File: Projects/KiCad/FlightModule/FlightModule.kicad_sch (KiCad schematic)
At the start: 45 parts, among them J1 Conn_01x04_Pin, J2 Conn_01x04_Socket, J3 Conn_01x02_Pin, J4 Conn_01x02_Pin, J5 Conn_01x02_Pin, J6 Conn_01x02_Pin, Q2 DTC143E, SW1 SW_Push, U1 NUCLEO-F303K8, U2 MCP2562-E-P, U3 TLP222A, U4 TLP222A, U5 24LC1025, U6 24LC1025

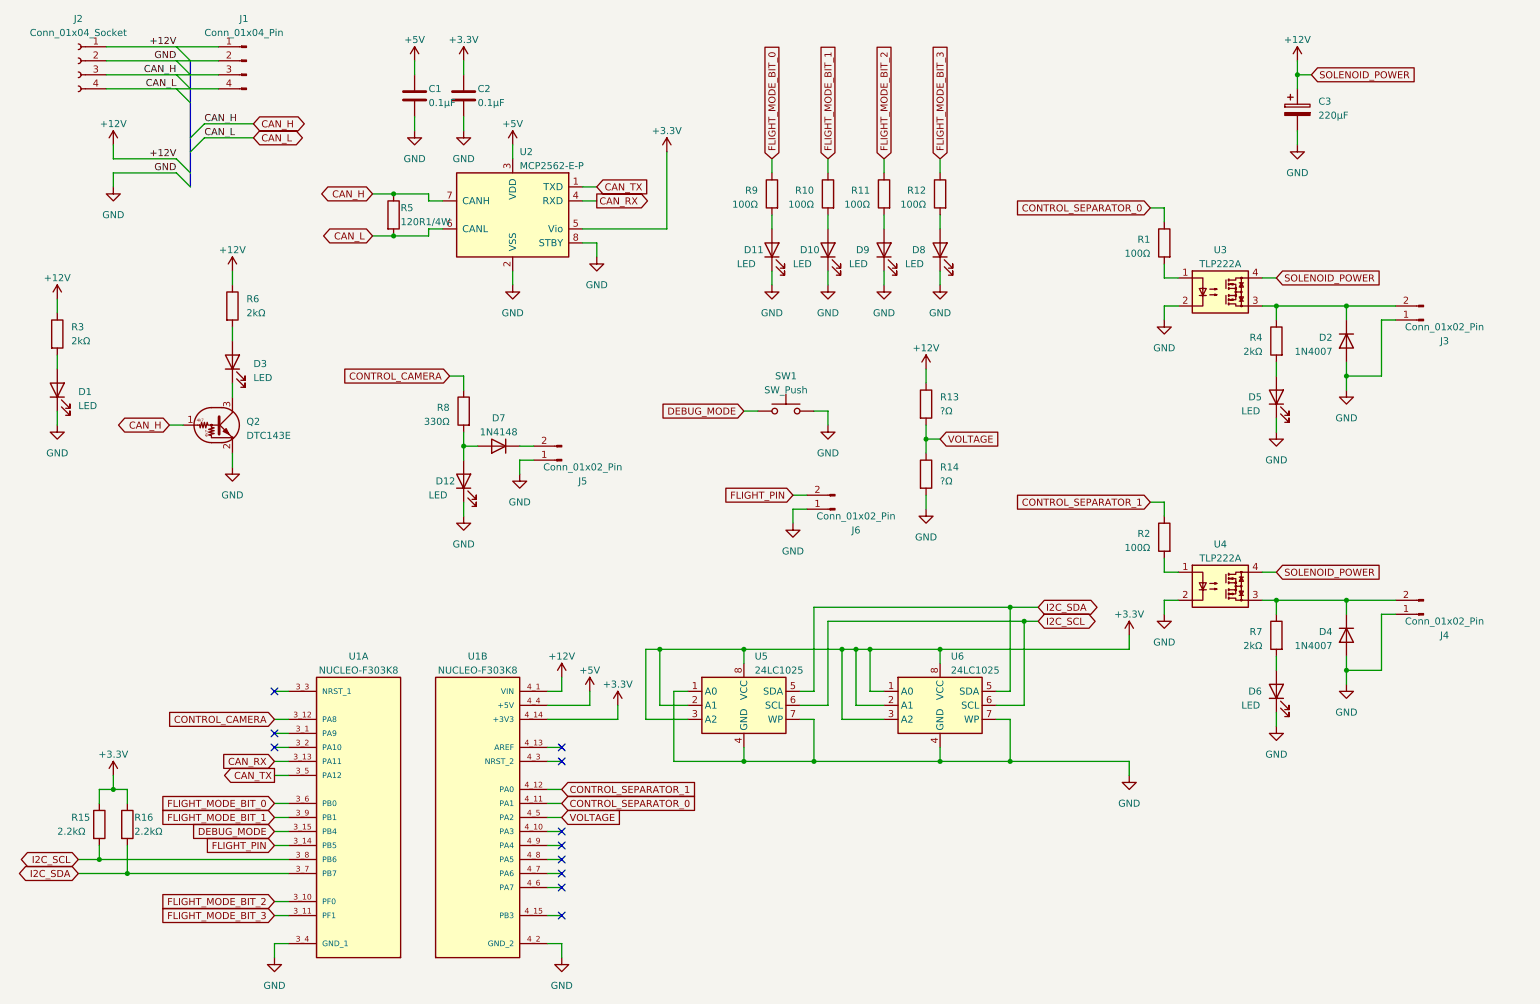
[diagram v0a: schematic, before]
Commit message: バスパワーのピンヘッダをP1.27からP2.54に修正
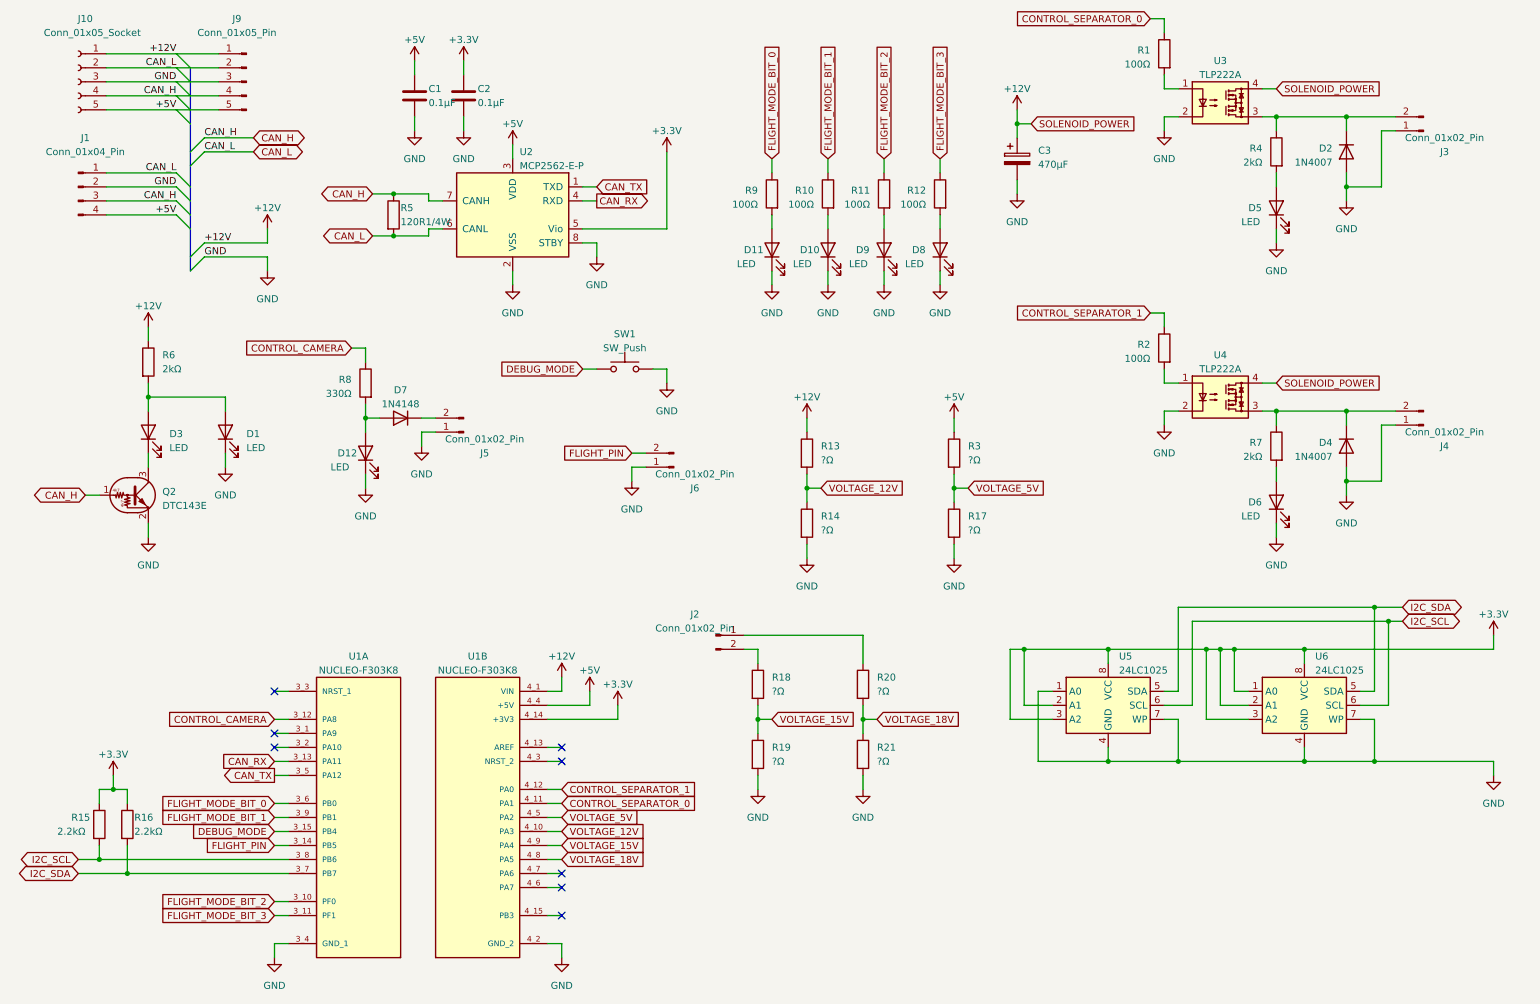
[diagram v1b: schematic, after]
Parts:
- removed J2: Conn_01x04_Socket, Connector_PinSocket_1.27mm:PinSocket_1x04_P1.27mm_Vertical, symbol Connector:Conn_01x04_Socket
- added J10: Conn_01x05_Socket, Connector_PinSocket_2.54mm:PinSocket_1x05_P2.54mm_Vertical, symbol Connector:Conn_01x05_Socket
- added J2: Conn_01x02_Pin, Connector_JST:JST_EH_S2B-EH_1x02_P2.50mm_Horizontal, symbol Connector:Conn_01x02_Pin
- added J9: Conn_01x05_Pin, Connector_PinHeader_2.54mm:PinHeader_1x05_P2.54mm_Vertical, symbol Connector:Conn_01x05_Pin
- added R17, R18, R19, R20, R21: ?Ω, Resistor_SMD:R_0805_2012Metric_Pad1.20x1.40mm_HandSolder, symbol Device:R
- C3: value 220μF -> 470μF; footprint Capacitor_SMD:CP_Elec_6.3x7.7 -> Capacitor_THT:CP_Radial_D10.0mm_P3.50mm
- J1: footprint Connector_PinHeader_1.27mm:PinHeader_1x04_P1.27mm_Vertical -> Connector_JST:JST_XH_S4B-XH-A_1x04_P2.50mm_Horizontal
- R3: value 2kΩ -> ?Ω
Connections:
- net +12V: now also J10.1 (Pin_1), J9.1 (Pin_1); no longer J1.1 (Pin_1), R3.1
- net +5V: now also J1.4 (Pin_4), R3.1, J10.5 (Pin_5), J9.5 (Pin_5)
- net CAN_H: now also J10.4 (Pin_4), J9.4 (Pin_4)
- net CAN_L: now also J1.1 (Pin_1), J10.2 (Pin_2), J9.2 (Pin_2); no longer J1.4 (Pin_4)
- net GND: now also J10.3 (Pin_3), J9.3 (Pin_3), R17.2, R19.2, R21.2
- net at D3.2 (A), R6.2: now also D1.2 (A)
- net VOLTAGE_5V: now reaches R3.2
- net VOLTAGE_5V: now also U1.4_5 (PA2), R17.1; no longer D1.2 (A)
- net VOLTAGE_12V: now reaches U1.4_10 (PA3)
- net VOLTAGE_12V: now also R13.2, R14.1
- net VOLTAGE_18V: now reaches U1.4_8 (PA5)
- net VOLTAGE_18V: now also R20.2, R21.1
- net VOLTAGE_15V: now reaches U1.4_9 (PA4)
- net VOLTAGE_15V: now also R18.2, R19.1
- removed net VOLTAGE: R13.2, R14.1, U1.4_5 (PA2)
- new net: J2.2 (Pin_2), R18.1
- new net: J2.1 (Pin_1), R20.1
- no-connect marks 11 -> 8
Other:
- moved on the sheet: C3, D1, D12, D2, D3, D4, D5, D6, D7, J3, J4, J5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

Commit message: RCを解決
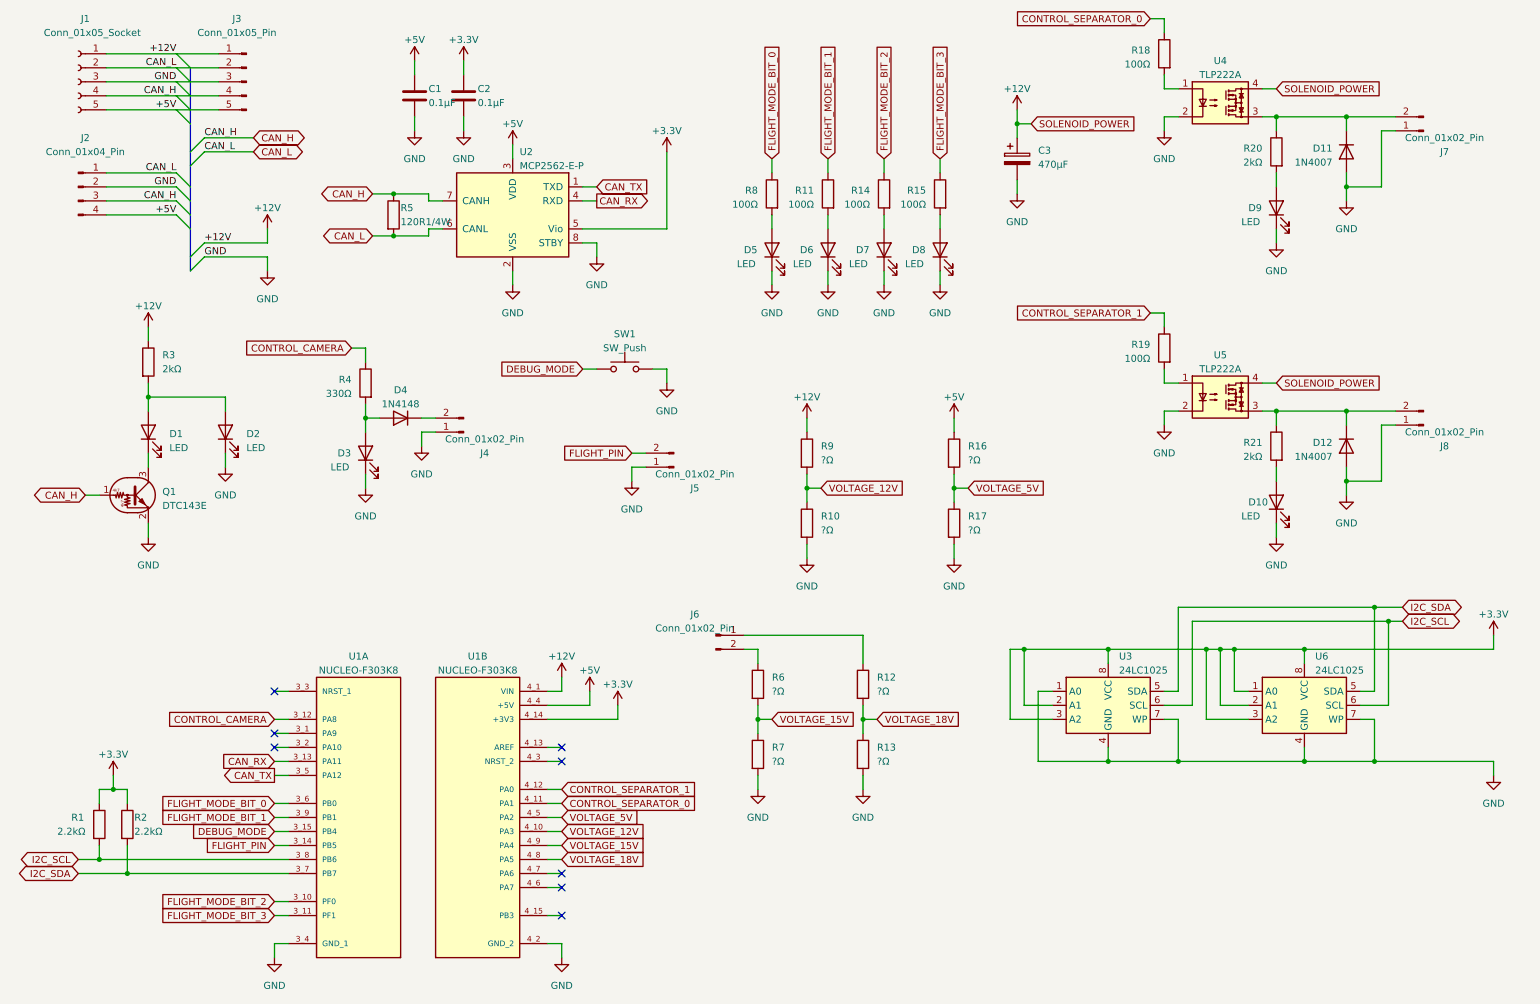
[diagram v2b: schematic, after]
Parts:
- renumbered D3 to D1, D6 to D10, D2 to D11, D4 to D12, D1 to D2, D12 to D3, D7 to D4, D11 to D5, D10 to D6, D9 to D7, D5 to D9, J10 to J1, J1 to J2, J9 to J3, J5 to J4, J6 to J5, J2 to J6, J3 to J7, J4 to J8, Q2 to Q1, R15 to R1, R14 to R10, R10 to R11, R20 to R12, R21 to R13, R11 to R14, R12 to R15, R3 to R16, R1 to R18, R2 to R19, R16 to R2, R4 to R20, R7 to R21, R6 to R3, R8 to R4, R18 to R6, R19 to R7, R9 to R8, R13 to R9, U5 to U3, U3 to U4, U4 to U5

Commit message: 計測モジュールとフライトモジュール終わり
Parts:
- removed D1: LED, LED_SMD:LED_1206_3216Metric_Pad1.42x1.75mm_HandSolder, symbol Device:LED
- removed Q1: DTC143E, Package_TO_SOT_THT:TO-92_Inline, symbol Transistor_BJT:DTC143E
- removed R1, R2: 2.2kΩ, Resistor_SMD:R_0805_2012Metric_Pad1.20x1.40mm_HandSolder, symbol Device:R
- removed U3, U6: 24LC1025, Package_DIP:DIP-8_W7.62mm, symbol Memory_EEPROM:24LC1025
- added D8, D9: LED, LED_SMD:LED_1206_3216Metric_Pad1.42x1.75mm_HandSolder, symbol Device:LED
- added R14, R15: 100Ω, Resistor_SMD:R_0805_2012Metric_Pad1.20x1.40mm_HandSolder, symbol Device:R
- added R18: 4.7kΩ, Resistor_SMD:R_0805_2012Metric_Pad1.20x1.40mm_HandSolder, symbol Device:R
- added SW2: SW_Push, Button_Switch_THT:SW_PUSH_6mm, symbol Switch:SW_Push
- added U5: MB85RS2MT, Package_DIP:DIP-8_W7.62mm, symbol Memory_NVRAM:MB85RS2MT
- J4, J7, J8: footprint Connector_JST:JST_EH_S2B-EH_1x02_P2.50mm_Horizontal -> Hirose_Connector:Hirose_DF1B
- J5: renamed from J6; footprint Connector_JST:JST_EH_S2B-EH_1x02_P2.50mm_Horizontal -> Hirose_Connector:Hirose_DF1B
- J6: renamed from J5; footprint Connector_JST:JST_EH_S2B-EH_1x02_P2.50mm_Horizontal -> Hirose_Connector:Hirose_DF1B
- SW1: footprint Button_Switch_SMD:SW_DIP_SPSTx01_Slide_6.7x4.1mm_W6.73mm_P2.54mm_LowProfile_JPin -> Button_Switch_THT:SW_PUSH_6mm
- renumbered D2 to D1, D9 to D10, D10 to D11, D11 to D12, D12 to D13, D3 to D2, D4 to D3, D5 to D4, D6 to D5, D7 to D6, D8 to D7, R3 to R1, R14 to R10, R9 to R11, R10 to R12, R15 to R13, R18 to R19, R4 to R2, R19 to R20, R20 to R21, R21 to R22, R5 to R3, R6 to R4, R7 to R5, R12 to R6, R13 to R7, R11 to R9, U4 to U3, U5 to U4
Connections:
- net +3.3V: now also R18.1, U5.8 (VDD)
- net CONTROL_SEPARATOR_0: now also U1.4_15 (PB3); no longer U1.4_11 (PA1)
- net DEBUG_MODE: now also SW1.2; no longer SW1.1
- net GND: now also SW1.1, D8.1 (K), D9.1 (K), SW2.1, U5.3 (~{WP}), U5.4 (GND), U5.7 (~{HOLD}); no longer SW1.2
- net VOLTAGE_12V: now also U1.4_5 (PA2); no longer U1.4_10 (PA3)
- net VOLTAGE_15V: now also U1.4_10 (PA3); no longer U1.4_9 (PA4)
- net VOLTAGE_18V: now also U1.4_9 (PA4); no longer U1.4_8 (PA5)
- net VOLTAGE_5V: now also U1.4_11 (PA1); no longer U1.4_5 (PA2)
- net at R4.1: now also J5.1 (Pin_1); no longer J5.2 (Pin_2)
- net SPI_MOSI: now reaches U1.4_6 (PA7)
- net SPI_MOSI: now also U5.5 (SI)
- net SPI_MISO: now reaches U1.4_7 (PA6)
- net SPI_MISO: now also U5.2 (SO)
- net at R6.1: now also J5.2 (Pin_2); no longer J5.1 (Pin_1)
- net CAN_RECEIVE_STATUS: now reaches U1.3_1 (PA9)
- net CAN_RECEIVE_STATUS: now also R14.1
- net CAN_SEND_STATUS: now reaches U1.3_2 (PA10)
- net CAN_SEND_STATUS: now also R15.1
- net I2C_SCL renamed DUMP_MODE
- net DUMP_MODE: now also SW2.2
- net I2C_SDA renamed SPI_CS_FRAM
- net SPI_CS_FRAM: now also R18.2, U5.1 (~{CS})
- new net: D9.2 (A), R15.2
- new net: D8.2 (A), R14.2
- new net SPI_SCLK: U1.4_8 (PA5), U5.6 (SCK)
- no-connect marks 8 -> 3
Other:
- moved on the sheet: C3, D1, D10, D11, D12, D13, D4, D5, D6, D7, J5, J6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
